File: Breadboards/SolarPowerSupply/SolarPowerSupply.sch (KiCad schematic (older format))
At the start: 49 parts, among them P101 CONN_01X04, P102 CONN_01X07, U101 bq25504, U102 TPS63051, U103 TPS63050

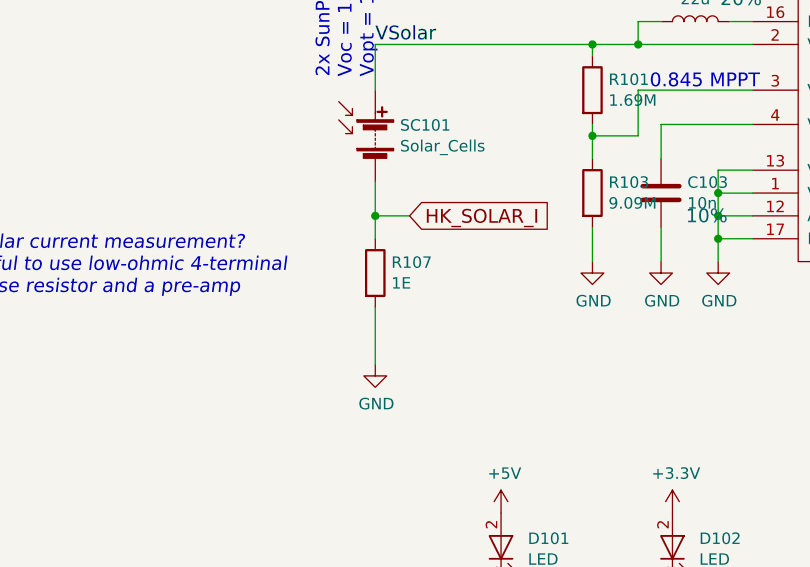
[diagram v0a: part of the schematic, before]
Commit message: Changes 1E Solar current res to 0E
Given the low internal resistance of the solar panels, a 1E resistance is too high.
For now just do a solder bridge
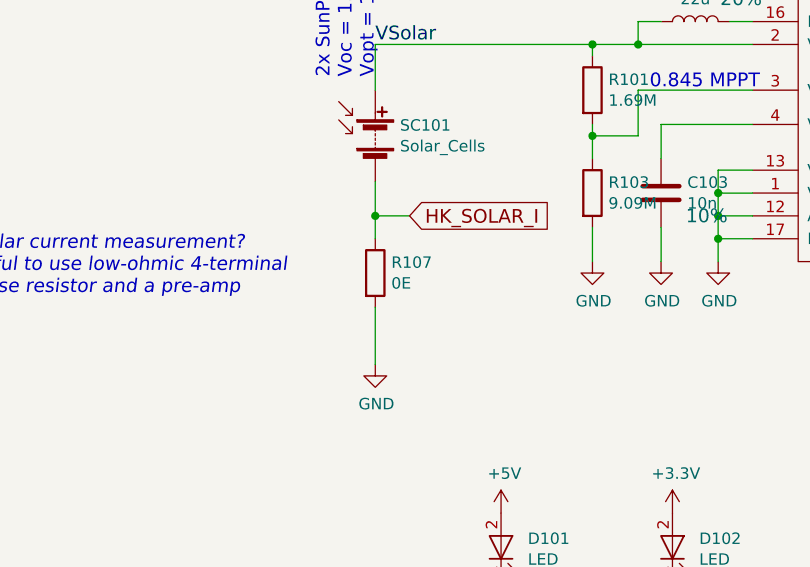
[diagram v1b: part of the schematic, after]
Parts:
- R107: value 1E -> 0E; MPN 603-RC1206DR-071RL -> (none)
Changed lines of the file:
@@
 P 1100 2600
 F 0 "R107" H 1170 2646 50  0000 L CNN
-F 1 "1E" H 1170 2555 50  0000 L CNN
+F 1 "0E" H 1170 2555 50  0000 L CNN
 F 2 "Resistors_SMD:R_1206_HandSoldering" V 1030 2600 50  0001 C CNN
 F 3 "" H 1100 2600 50  0001 C CNN
-F 4 "603-RC1206DR-071RL" H 0   0   60  0001 C CNN "MPN"
 	1    1100 2600
 	1    0    0    -1

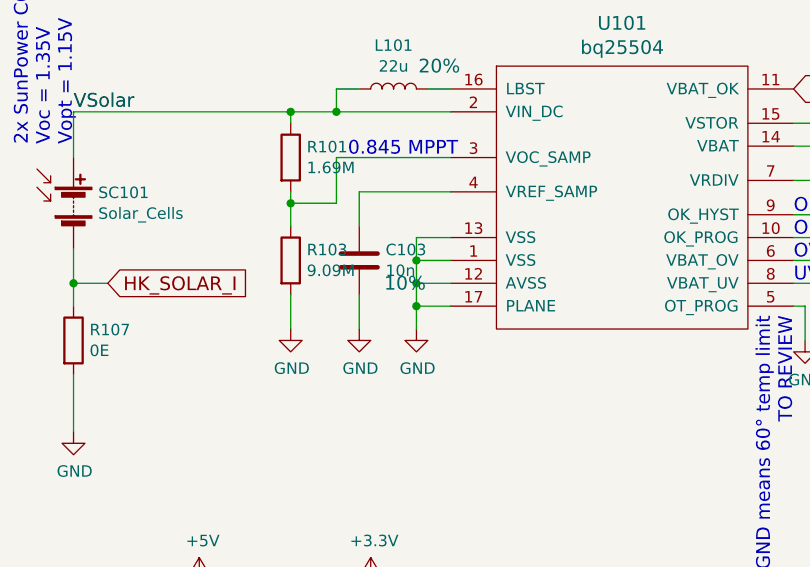
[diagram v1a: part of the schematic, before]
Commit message: Changes CREF to low leakage capacitor
The 10nF CREF capacitor used by the bq25504 needs to be of low leakage quality,
as it needs to hold the input voltage reference for up to 16s. With the current
capacitor (no-name) the voltage drops by approx. 25% during these 16s.
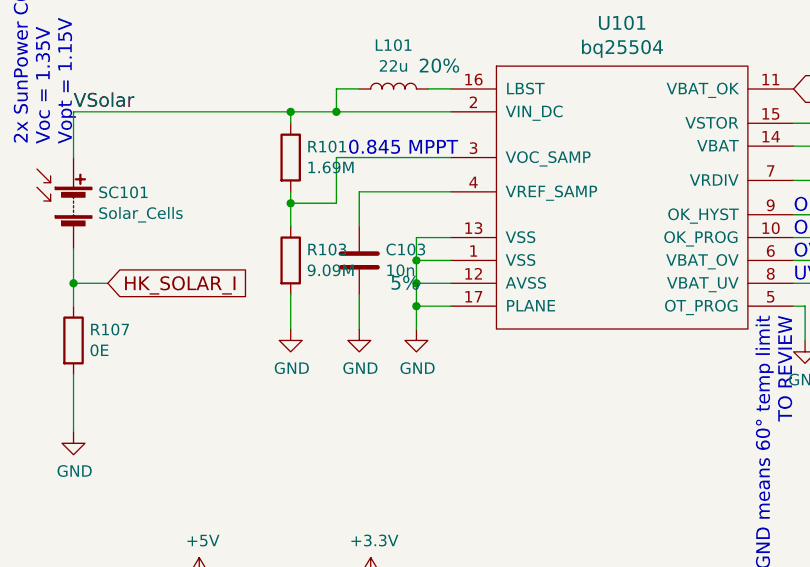
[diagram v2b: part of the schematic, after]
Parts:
- C103: MPN (none) -> 80-C0603C103J3G; Tolerance 10% -> 5%
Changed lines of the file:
@@
 F 2 "Capacitors_SMD:C_0603_HandSoldering" H 2388 2100 50  0001 C CNN
 F 3 "" H 2350 2250 50  0001 C CNN
-F 4 "10%" H 2550 2150 60  0000 C CNN "Tolerance"
+F 4 "5%" H 2550 2150 60  0000 C CNN "Tolerance"
+F 5 "80-C0603C103J3G" H 2350 2250 60  0001 C CNN "MPN"
 	1    2350 2250
 	1    0    0    -1
